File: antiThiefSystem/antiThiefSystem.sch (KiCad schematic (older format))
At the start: 5 parts, among them U1 74LS04, U2 74LS76, U3 74LS08, U4 74LS08, U5 74LS32

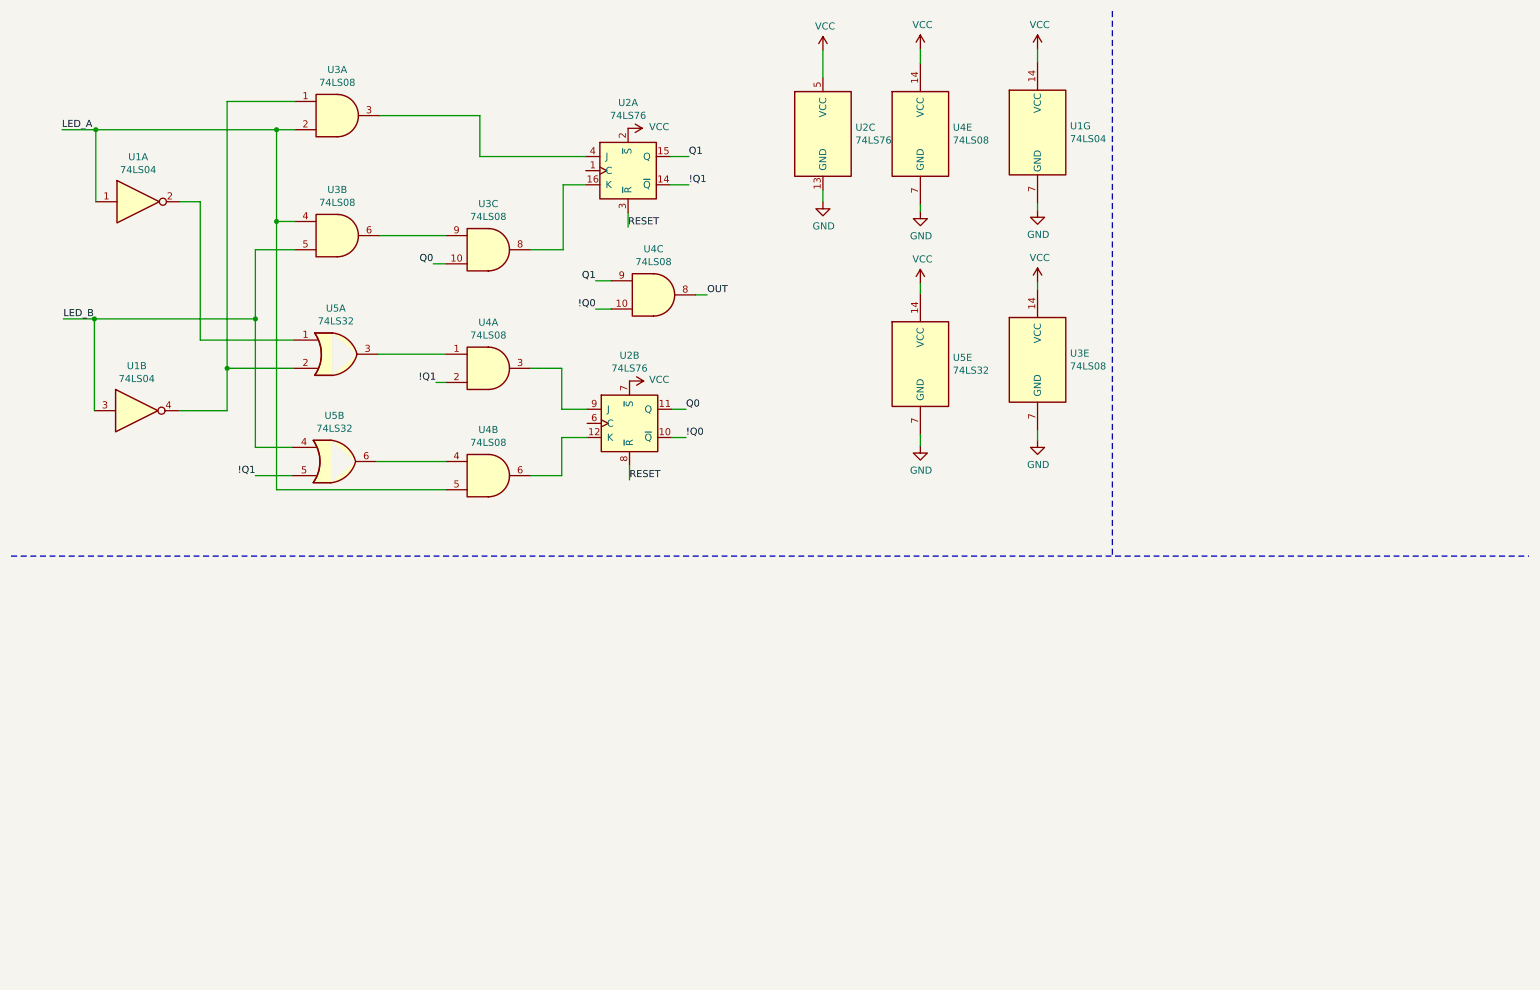
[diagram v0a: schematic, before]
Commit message: Add power block, clock block and input block
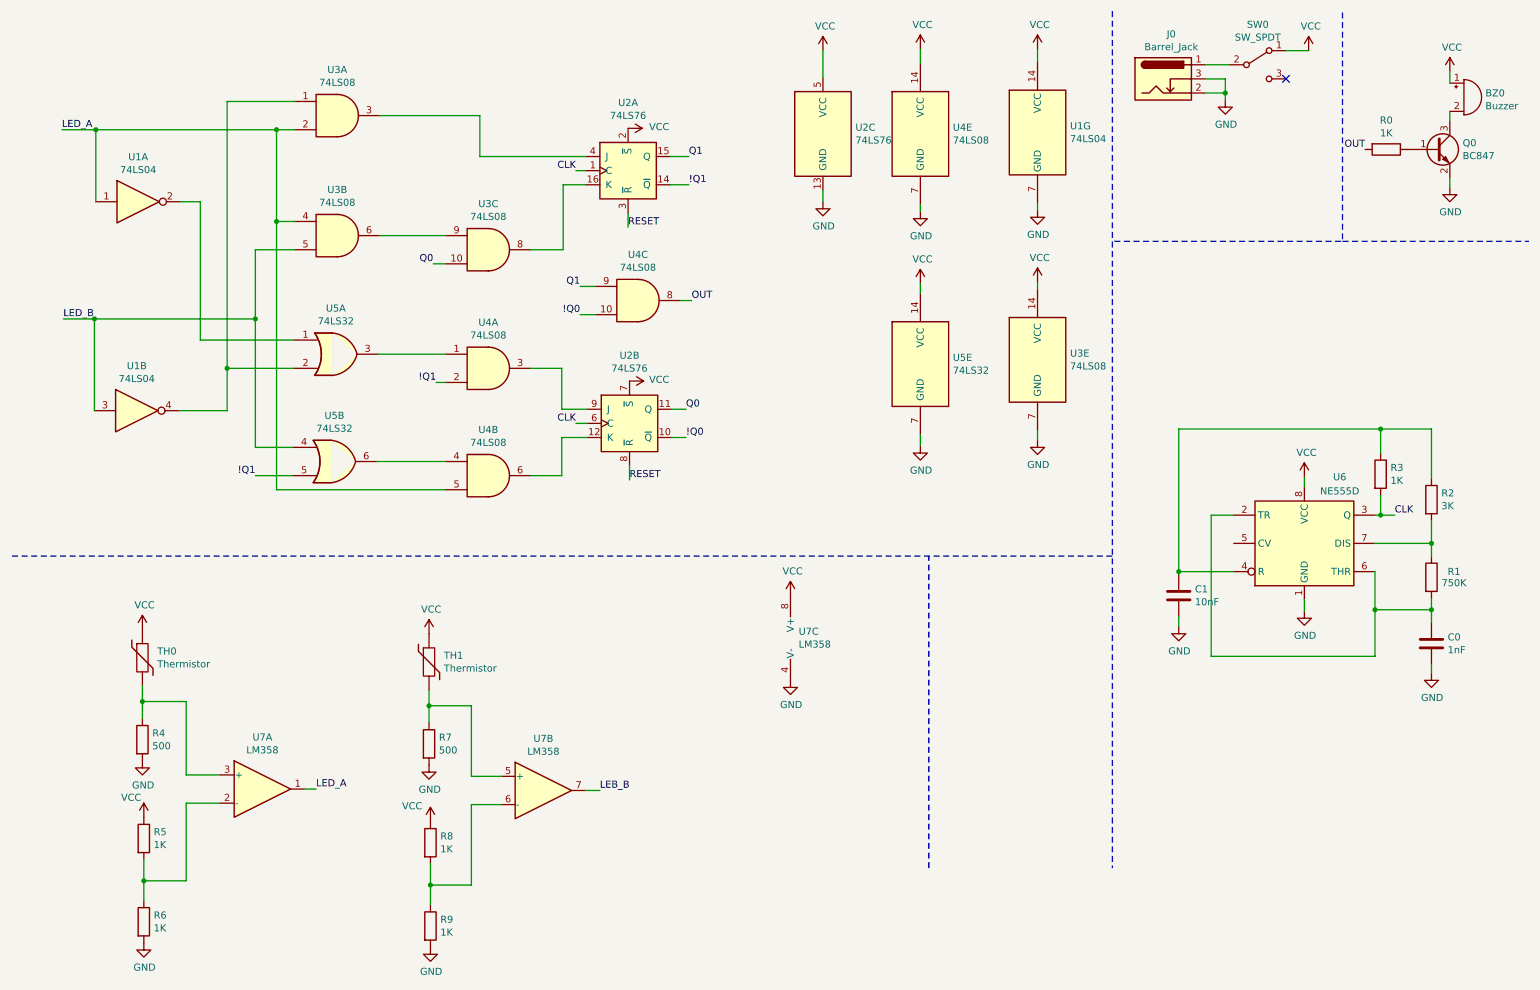
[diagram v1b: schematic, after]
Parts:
- added BZ0: Buzzer, symbol Device:Buzzer
- added C0: 1nF, symbol Device:C
- added C1: 10nF, symbol Device:C
- added J0: Barrel_Jack, symbol Connector:Barrel_Jack_Switch
- added Q0: BC847, Package_TO_SOT_SMD:SOT-23, symbol Transistor_BJT:BC847
- added R0, R3, R5, R6, R8, R9: 1K, symbol Device:R
- added R1: 750K, symbol Device:R
- added R2: 3K, symbol Device:R
- added R4, R7: 500, symbol Device:R
- added SW0: SW_SPDT, symbol Switch:SW_SPDT
- added TH0, TH1: Thermistor, symbol Device:Thermistor
- added U6: NE555D, Package_SO:SOIC-8_3.9x4.9mm_P1.27mm, symbol Timer:NE555D
- added U7: LM358, symbol Amplifier_Operational:LM358
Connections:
- net GND: now also C0.2, C1.1, J0.2, J0.3, Q0.2 (E), R4.2, R6.2, R7.2, R9.2, U6.1 (GND), U7.4 (V-)
- net LED_A: now also U7.1
- net OUT: now also R0.2
- net VCC: now also BZ0.1 (-), R5.1, R8.1, SW0.1 (A), TH0.1, TH1.1, U6.8 (VCC), U7.8 (V+)
- net CLK: now reaches U2.1 (C)
- net CLK: now also U2.6 (C), R3.2, U6.3 (Q)
- new net: J0.1, SW0.2 (B)
- new net: Q0.1 (B), R0.1
- new net: BZ0.2 (+), Q0.3 (C)
- new net: C0.1, R1.2, U6.2 (TR), U6.6 (THR)
- new net: C1.2, R2.1, R3.1, U6.4 (R)
- new net: R1.1, R2.2, U6.7 (DIS)
- new net: R5.2, R6.1, U7.2 (-)
- new net: R4.1, TH0.2, U7.3 (+)
- new net: R7.1, TH1.2, U7.5 (+)
- new net: R8.2, R9.1, U7.6 (-)
- new net LEB_B: U7.7
- no-connect marks 0 -> 1
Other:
- moved on the sheet: U4C

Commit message: Draw PCB not completely
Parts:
- added J1: 2272-T4, Connector_PinSocket_2.54mm:PinSocket_1x07_P2.54mm_Vertical, symbol Connector:Conn_01x07_Female
- BZ0: footprint (none) -> Buzzer_Beeper:Buzzer_12x9.5RM7.6
- C0, C1: footprint (none) -> Capacitor_SMD:C_1206_3216Metric
- J0: footprint (none) -> Connector_BarrelJack:BarrelJack_Horizontal
- Q0: value BC847 -> 2SC1815; footprint Package_TO_SOT_SMD:SOT-23 -> Package_TO_SOT_THT:TO-92L_Inline_Wide
- R0, R1, R2, R3, R4, R5, R6, R7, R8, R9: footprint (none) -> Resistor_SMD:R_1206_3216Metric
- SW0: footprint (none) -> digitalSystemBoard:SS-12D11
- TH0, TH1: footprint (none) -> Connector_PinSocket_2.54mm:PinSocket_1x02_P2.54mm_Vertical
- U1, U3, U4, U5: footprint (none) -> Package_DIP:DIP-14_W7.62mm_Socket
- U2: footprint (none) -> Package_DIP:DIP-16_W7.62mm_Socket
- U6: footprint Package_SO:SOIC-8_3.9x4.9mm_P1.27mm -> Package_DIP:DIP-8_W7.62mm_Socket
- U7: footprint (none) -> Package_DIP:DIP-8_W7.62mm_Socket
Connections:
- net LEB_B is gone; now on net LED_B: U7.7
- net GND: now also J1.5 (Pin_5)
- net RESET: now also J1.4 (Pin_4)
- net VCC: now also J1.7 (Pin_7)
- no-connect marks 1 -> 6

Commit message: Finish PCB
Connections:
- net VCC: now also SW0.3 (C); no longer SW0.1 (A)
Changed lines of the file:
@@
 L power:VCC #PWR0113
 U 1 1 615D62D1
-P 9660 750
-F 0 "#PWR0113" H 9660 600 50  0001 C CNN
-F 1 "VCC" H 9675 923 50  0000 C CNN
-F 2 "" H 9660 750 50  0001 C CNN
-F 3 "" H 9660 750 50  0001 C CNN
-	1    9660 750
+P 9650 950
+F 0 "#PWR0113" H 9650 800 50  0001 C CNN
+F 1 "VCC" H 9665 1123 50  0000 C CNN
+F 2 "" H 9650 950 50  0001 C CNN
+F 3 "" H 9650 950 50  0001 C CNN
+	1    9650 950
 	1    0    0    -1
 $EndComp
@@
 $EndComp
 Wire Wire Line
-	9500 750  9660 750
-Wire Wire Line
 	8930 850  9100 850
 Connection ~ 9070 1050
@@
 F 3 "" H 9070 1100 50  0001 C CNN
 	1    9070 1100
-	1    0    0    -1
-$EndComp
-NoConn ~ 9500 950
-$Comp
-L Switch:SW_SPDT SW0
-U 1 1 615D3337
-P 9300 850
-F 0 "SW0" H 9300 1135 50  0000 C CNN
-F 1 "SW_SPDT" H 9300 1044 50  0000 C CNN
-F 2 "digitalSystemBoard:SS-12D11" H 9300 850 50  0001 C CNN
-F 3 "~" H 9300 850 50  0001 C CNN
-	1    9300 850
 	1    0    0    -1
 $EndComp
@@
 Wire Wire Line
 	2630 5980 2550 5980
+$Comp
+L Switch:SW_SPDT SW0
+U 1 1 615D3337
+P 9300 850
+F 0 "SW0" H 9300 1135 50  0000 C CNN
+F 1 "SW_SPDT" H 9300 1044 50  0000 C CNN
+F 2 "digitalSystemBoard:SS-12D11" H 9300 850 50  0001 C CNN
+F 3 "~" H 9300 850 50  0001 C CNN
+	1    9300 850
+	1    0    0    -1
+$EndComp
+NoConn ~ 9500 750
+Wire Wire Line
+	9500 950  9650 950
 $EndSCHEMATC
